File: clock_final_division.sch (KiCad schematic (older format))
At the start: 7 parts, among them SW2 SW_Rotary12, U10 74LVC161, U11 74LVC74, U9 74LVC74

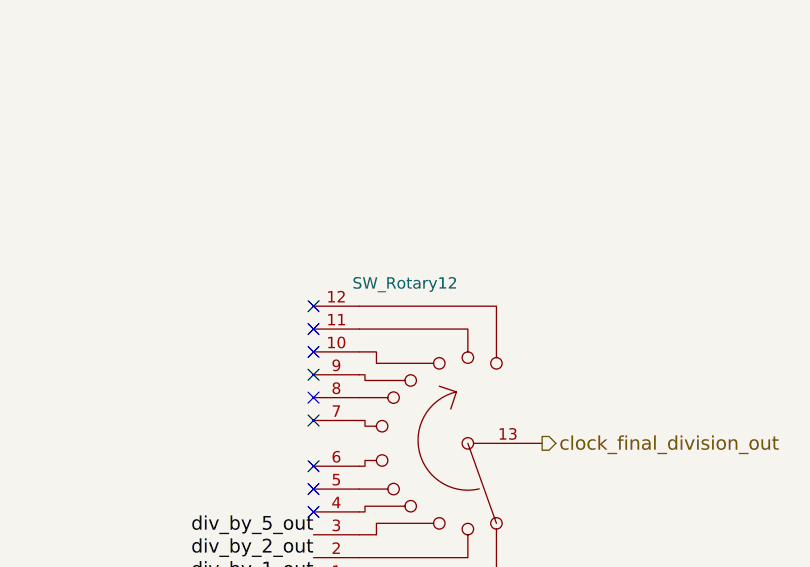
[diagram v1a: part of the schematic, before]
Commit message: R2 PCB rotary switches closer to middle of board
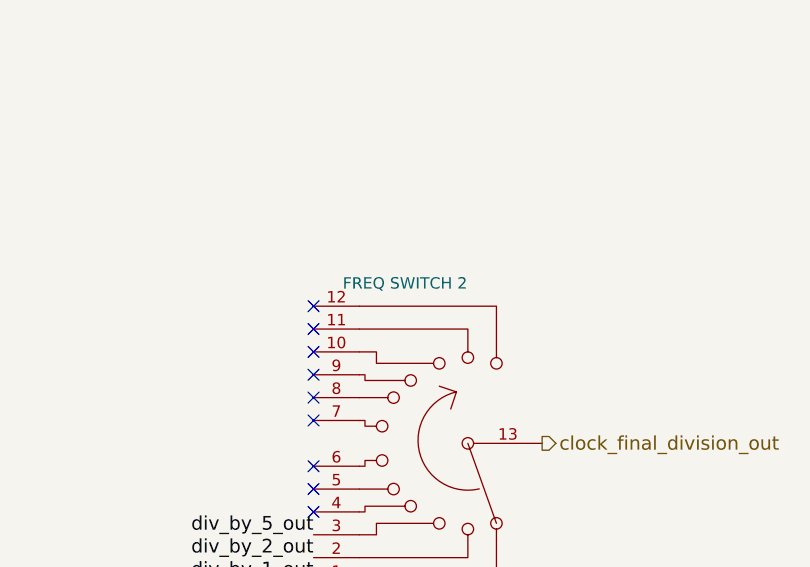
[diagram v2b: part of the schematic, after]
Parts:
- SW2: value SW_Rotary12 -> FREQ SWITCH 2; Distributor (none) -> Mouser; Distributor PN (none) -> 633-MRK112A; Manufacturer (none) -> NKK; Manufacturer PN (none) -> MRK112-A; URL (none) -> http://www.mouser.com/Search/ProductDetail.aspx?R=MRK112-Av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; Unit Price (none) -> 11.80
- U10: Distributor (none) -> Mouser; Distributor PN (none) -> 771-LVC161D118; Manufacturer (none) -> Nexperia; Manufacturer PN (none) -> 4LVC161D118; URL (none) -> http://www.mouser.com/Search/ProductDetail.aspx?R=74LVC161D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; Unit Price (none) -> 0.61
- U11, U9: Distributor (none) -> Mouser; Distributor PN (none) -> 595-SN74LVC74ADR; Manufacturer (none) -> TI; Manufacturer PN (none) -> SN74LVC74ADR; URL (none) -> http://www.mouser.com/Search/ProductDetail.aspx?R=SN74LVC74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; Unit Price (none) -> 0.40
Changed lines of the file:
@@
 encoding utf-8
 Sheet 3 6
-Title ""
+Title "calbox final frequency division"
 Date ""
 Rev ""
@@
 clock
 $Comp
-L GND #PWR33
+L GND #PWR032
 U 1 1 58C209C7
 P 1300 1500
-F 0 "#PWR33" H 1300 1250 50  0001 C CNN
+F 0 "#PWR032" H 1300 1250 50  0001 C CNN
 F 1 "GND" H 1300 1350 50  0000 C CNN
 F 2 "" H 1300 1500 50  0000 C CNN
@@
 $EndComp
 $Comp
-L GND #PWR41
+L GND #PWR033
 U 1 1 58C29AA8
 P 3800 1950
-F 0 "#PWR41" H 3800 1700 50  0001 C CNN
+F 0 "#PWR033" H 3800 1700 50  0001 C CNN
 F 1 "GND" H 3800 1800 50  0000 C CNN
 F 2 "" H 3800 1950 50  0000 C CNN
@@
 $EndComp
 $Comp
-L GND #PWR39
+L GND #PWR034
 U 1 1 58C29ADA
 P 3700 4650
-F 0 "#PWR39" H 3700 4400 50  0001 C CNN
+F 0 "#PWR034" H 3700 4400 50  0001 C CNN
 F 1 "GND" H 3700 4500 50  0000 C CNN
 F 2 "" H 3700 4650 50  0000 C CNN
@@
 $EndComp
 $Comp
-L GND #PWR47
+L GND #PWR035
 U 1 1 58C29B03
 P 7500 2950
-F 0 "#PWR47" H 7500 2700 50  0001 C CNN
+F 0 "#PWR035" H 7500 2700 50  0001 C CNN
 F 1 "GND" H 7500 2800 50  0000 C CNN
 F 2 "" H 7500 2950 50  0000 C CNN
@@
 clock
 $Comp
-L 74LVC161 U10
-U 1 1 58C76F32
-P 2300 1900
-F 0 "U10" H 2350 2000 50  0000 C CNN
-F 1 "74LVC161" H 2400 1700 50  0000 C CNN
-F 2 "SMD_Packages:SO-16-N" H 2300 1900 50  0001 C CNN
-F 3 "" H 2300 1900 50  0000 C CNN
-	1    2300 1900
-	1    0    0    -1
-$EndComp
-$Comp
 L 74LVC74 U9
 U 1 1 58C77242
@@
 F 1 "74LVC74" H 2300 3205 50  0000 C CNN
 F 2 "SMD_Packages:SOIC-14_N" H 2000 3500 50  0001 C CNN
-F 3 "" H 2000 3500 50  0000 C CNN
+F 3 "http://www.ti.com/lit/ds/symlink/sn74lvc74a.pdf" H 2000 3500 50  0001 C CNN
+F 4 "TI" H 2000 3500 60  0001 C CNN "Manufacturer"
+F 5 "SN74LVC74ADR" H 2000 3500 60  0001 C CNN "Manufacturer PN"
+F 6 "Mouser" H 2000 3500 60  0001 C CNN "Distributor"
+F 7 "595-SN74LVC74ADR" H 2000 3500 60  0001 C CNN "Distributor PN"
+F 8 "http://www.mouser.com/Search/ProductDetail.aspx?R=SN74LVC74ADRvirtualkey59500000virtualkey595-SN74LVC74ADR" H 2000 3500 60  0001 C CNN "URL"
+F 9 "0.40" H 2000 3500 60  0001 C CNN "Unit Price"
 	1    2000 3500
-	1    0    0    -1
-$EndComp
-$Comp
-L 74LVC74 U9
-U 2 1 58C7727E
-P 2000 5300
-F 0 "U9" H 2150 5600 50  0000 C CNN
-F 1 "74LVC74" H 2300 5005 50  0000 C CNN
-F 2 "SMD_Packages:SOIC-14_N" H 2000 5300 50  0001 C CNN
-F 3 "" H 2000 5300 50  0000 C CNN
-	2    2000 5300
-	1    0    0    -1
-$EndComp
-$Comp
-L 74LVC74 U11
-U 1 1 58C77320
-P 5900 1800
-F 0 "U11" H 6050 2100 50  0000 C CNN
-F 1 "74LVC74" H 6200 1505 50  0000 C CNN
-F 2 "SMD_Packages:SOIC-14_N" H 5900 1800 50  0001 C CNN
-F 3 "" H 5900 1800 50  0000 C CNN
-	1    5900 1800
-	1    0    0    -1
-$EndComp
-$Comp
-L 74LVC74 U11
-U 2 1 58C77357
-P 5900 3600
-F 0 "U11" H 6050 3900 50  0000 C CNN
-F 1 "74LVC74" H 6200 3305 50  0000 C CNN
-F 2 "SMD_Packages:SOIC-14_N" H 5900 3600 50  0001 C CNN
-F 3 "" H 5900 3600 50  0000 C CNN
-	2    5900 3600
 	1    0    0    -1
 $EndComp
@@
 P 8950 5300
 F 0 "SW2" H 8950 6000 50  0000 C CNN
-F 1 "SW_Rotary12" H 8950 4600 50  0000 C CNN
+F 1 "FREQ SWITCH 2" H 8950 4600 50  0000 C CNN
 F 2 "calbox:SW_ROTARY_SP12T_MRK112" H 8750 6000 50  0001 C CNN
-F 3 "" H 8750 6000 50  0001 C CNN
+F 3 "http://www.mouser.com/ds/2/295/MRlogicLevel-9701.pdf" H 8750 6000 50  0001 C CNN
+F 4 "NKK" H 8950 5300 60  0001 C CNN "Manufacturer"
+F 5 "MRK112-A" H 8950 5300 60  0001 C CNN "Manufacturer PN"
+F 6 "Mouser" H 8950 5300 60  0001 C CNN "Distributor"
+F 7 "633-MRK112A" H 8950 5300 60  0001 C CNN "Distributor PN"
+F 8 "http://www.mouser.com/Search/ProductDetail.aspx?R=MRK112-Avirtualkey63300000virtualkey633-MRK112A" H 8950 5300 60  0001 C CNN "URL"
+F 9 "11.80" H 8950 5300 60  0001 C CNN "Unit Price"
 	1    8950 5300
 	-1   0    0    1
@@
 NoConn ~ 8550 4700
 $Comp
-L VCC #PWR34
+L VCC #PWR036
 U 1 1 58C81CC4
 P 1800 4000
-F 0 "#PWR34" H 1800 3850 50  0001 C CNN
+F 0 "#PWR036" H 1800 3850 50  0001 C CNN
 F 1 "VCC" H 1800 4150 50  0000 C CNN
 F 2 "" H 1800 4000 50  0000 C CNN
@@
 $EndComp
 $Comp
-L VCC #PWR36
+L VCC #PWR037
 U 1 1 58C81F23
 P 2000 2950
-F 0 "#PWR36" H 2000 2800 50  0001 C CNN
+F 0 "#PWR037" H 2000 2800 50  0001 C CNN
 F 1 "VCC" H 2000 3100 50  0000 C CNN
 F 2 "" H 2000 2950 50  0000 C CNN
@@
 $EndComp
 $Comp
-L VCC #PWR37
+L VCC #PWR038
 U 1 1 58C81F49
 P 2000 4750
-F 0 "#PWR37" H 2000 4600 50  0001 C CNN
+F 0 "#PWR038" H 2000 4600 50  0001 C CNN
 F 1 "VCC" H 2000 4900 50  0000 C CNN
 F 2 "" H 2000 4750 50  0000 C CNN
@@
 $EndComp
 $Comp
-L VCC #PWR35
+L VCC #PWR039
 U 1 1 58C81F6F
 P 1800 5800
-F 0 "#PWR35" H 1800 5650 50  0001 C CNN
+F 0 "#PWR039" H 1800 5650 50  0001 C CNN
 F 1 "VCC" H 1800 5950 50  0000 C CNN
 F 2 "" H 1800 5800 50  0000 C CNN
@@
 $EndComp
 $Comp
-L VCC #PWR32
+L VCC #PWR040
 U 1 1 58C83204
 P 850 1900
-F 0 "#PWR32" H 850 1750 50  0001 C CNN
+F 0 "#PWR040" H 850 1750 50  0001 C CNN
 F 1 "VCC" H 850 2050 50  0000 C CNN
 F 2 "" H 850 1900 50  0000 C CNN
@@
 $EndComp
 $Comp
-L VCC #PWR40
+L VCC #PWR041
 U 1 1 58C8322A
 P 3800 1650
-F 0 "#PWR40" H 3800 1500 50  0001 C CNN
+F 0 "#PWR041" H 3800 1500 50  0001 C CNN
 F 1 "VCC" H 3800 1800 50  0000 C CNN
 F 2 "" H 3800 1650 50  0000 C CNN
@@
 $EndComp
 $Comp
-L VCC #PWR38
+L VCC #PWR042
 U 1 1 58C83250
 P 3700 4350
-F 0 "#PWR38" H 3700 4200 50  0001 C CNN
+F 0 "#PWR042" H 3700 4200 50  0001 C CNN
 F 1 "VCC" H 3700 4500 50  0000 C CNN
 F 2 "" H 3700 4350 50  0000 C CNN
@@
 $EndComp
 $Comp
-L VCC #PWR46
+L VCC #PWR043
 U 1 1 58C83276
 P 7500 2650
-F 0 "#PWR46" H 7500 2500 50  0001 C CNN
+F 0 "#PWR043" H 7500 2500 50  0001 C CNN
 F 1 "VCC" H 7500 2800 50  0000 C CNN
 F 2 "" H 7500 2650 50  0000 C CNN
@@
 $EndComp
 $Comp
-L VCC #PWR45
+L VCC #PWR044
 U 1 1 58C8329C
 P 5900 3050
-F 0 "#PWR45" H 5900 2900 50  0001 C CNN
+F 0 "#PWR044" H 5900 2900 50  0001 C CNN
 F 1 "VCC" H 5900 3200 50  0000 C CNN
 F 2 "" H 5900 3050 50  0000 C CNN
@@
 $EndComp
 $Comp
-L VCC #PWR44
+L VCC #PWR045
 U 1 1 58C832C2
 P 5900 1250
-F 0 "#PWR44" H 5900 1100 50  0001 C CNN
+F 0 "#PWR045" H 5900 1100 50  0001 C CNN
 F 1 "VCC" H 5900 1400 50  0000 C CNN
 F 2 "" H 5900 1250 50  0000 C CNN
@@
 $EndComp
 $Comp
-L VCC #PWR43
+L VCC #PWR046
 U 1 1 58C8357B
 P 5700 4100
-F 0 "#PWR43" H 5700 3950 50  0001 C CNN
+F 0 "#PWR046" H 5700 3950 50  0001 C CNN
 F 1 "VCC" H 5700 4250 50  0000 C CNN
 F 2 "" H 5700 4100 50  0000 C CNN
@@
 $EndComp
 $Comp
-L VCC #PWR42
+L VCC #PWR047
 U 1 1 58C835A1
 P 5700 2300
-F 0 "#PWR42" H 5700 2150 50  0001 C CNN
+F 0 "#PWR047" H 5700 2150 50  0001 C CNN
 F 1 "VCC" H 5700 2450 50  0000 C CNN
 F 2 "" H 5700 2300 50  0000 C CNN
@@
 	1    0    0    -1
 $EndComp
+$Comp
+L 74LVC161 U10
+U 1 1 58D05156
+P 2300 1900
+F 0 "U10" H 2350 2000 50  0000 C CNN
+F 1 "74LVC161" H 2400 1700 50  0000 C CNN
+F 2 "SMD_Packages:SO-16-N" H 2300 1900 50  0001 C CNN
+F 3 "http://www.mouser.com/ds/2/302/74LVC161-839606.pdf" H 2300 1900 50  0001 C CNN
+F 4 "Nexperia" H 2300 1900 60  0001 C CNN "Manufacturer"
+F 5 "4LVC161D118" H 2300 1900 60  0001 C CNN "Manufacturer PN"
+F 6 "Mouser" H 2300 1900 60  0001 C CNN "Distributor"
+F 7 "771-LVC161D118" H 2300 1900 60  0001 C CNN "Distributor PN"
+F 8 "http://www.mouser.com/Search/ProductDetail.aspx?R=74LVC161D%2c118virtualkey66800000virtualkey771-LVC161D118" H 2300 1900 60  0001 C CNN "URL"
+F 9 "0.61" H 2300 1900 60  0001 C CNN "Unit Price"
+	1    2300 1900
+	1    0    0    -1
+$EndComp
+$Comp
+L 74LVC74 U9
+U 2 1 58D05572
+P 2000 5300
+F 0 "U9" H 2150 5600 50  0000 C CNN
+F 1 "74LVC74" H 2300 5005 50  0000 C CNN
+F 2 "SMD_Packages:SOIC-14_N" H 2000 5300 50  0001 C CNN
+F 3 "http://www.ti.com/lit/ds/symlink/sn74lvc74a.pdf" H 2000 5300 50  0001 C CNN
+F 4 "TI" H 2000 5300 60  0001 C CNN "Manufacturer"
+F 5 "SN74LVC74ADR" H 2000 5300 60  0001 C CNN "Manufacturer PN"
+F 6 "Mouser" H 2000 5300 60  0001 C CNN "Distributor"
+F 7 "595-SN74LVC74ADR" H 2000 5300 60  0001 C CNN "Distributor PN"
+F 8 "http://www.mouser.com/Search/ProductDetail.aspx?R=SN74LVC74ADRvirtualkey59500000virtualkey595-SN74LVC74ADR" H 2000 5300 60  0001 C CNN "URL"
+F 9 "0.40" H 2000 5300 60  0001 C CNN "Unit Price"
+	2    2000 5300
+	1    0    0    -1
+$EndComp
+$Comp
+L 74LVC74 U11
+U 1 1 58D056BC
+P 5900 1800
+F 0 "U11" H 6050 2100 50  0000 C CNN
+F 1 "74LVC74" H 6200 1505 50  0000 C CNN
+F 2 "SMD_Packages:SOIC-14_N" H 5900 1800 50  0001 C CNN
+F 3 "http://www.ti.com/lit/ds/symlink/sn74lvc74a.pdf" H 5900 1800 50  0001 C CNN
+F 4 "TI" H 5900 1800 60  0001 C CNN "Manufacturer"
+F 5 "SN74LVC74ADR" H 5900 1800 60  0001 C CNN "Manufacturer PN"
+F 6 "Mouser" H 5900 1800 60  0001 C CNN "Distributor"
+F 7 "595-SN74LVC74ADR" H 5900 1800 60  0001 C CNN "Distributor PN"
+F 8 "http://www.mouser.com/Search/ProductDetail.aspx?R=SN74LVC74ADRvirtualkey59500000virtualkey595-SN74LVC74ADR" H 5900 1800 60  0001 C CNN "URL"
+F 9 "0.40" H 5900 1800 60  0001 C CNN "Unit Price"
+	1    5900 1800
+	1    0    0    -1
+$EndComp
+$Comp
+L 74LVC74 U11
+U 2 1 58D05720
+P 5900 3600
+F 0 "U11" H 6050 3900 50  0000 C CNN
+F 1 "74LVC74" H 6200 3305 50  0000 C CNN
+F 2 "SMD_Packages:SOIC-14_N" H 5900 3600 50  0001 C CNN
+F 3 "http://www.ti.com/lit/ds/symlink/sn74lvc74a.pdf" H 5900 3600 50  0001 C CNN
+F 4 "TI" H 5900 3600 60  0001 C CNN "Manufacturer"
+F 5 "SN74LVC74ADR" H 5900 3600 60  0001 C CNN "Manufacturer PN"
+F 6 "Mouser" H 5900 3600 60  0001 C CNN "Distributor"
+F 7 "595-SN74LVC74ADR" H 5900 3600 60  0001 C CNN "Distributor PN"
+F 8 "http://www.mouser.com/Search/ProductDetail.aspx?R=SN74LVC74ADRvirtualkey59500000virtualkey595-SN74LVC74ADR" H 5900 3600 60  0001 C CNN "URL"
+F 9 "0.40" H 5900 3600 60  0001 C CNN "Unit Price"
+	2    5900 3600
+	1    0    0    -1
+$EndComp

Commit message: update switch models in library, rotate final clock division switch
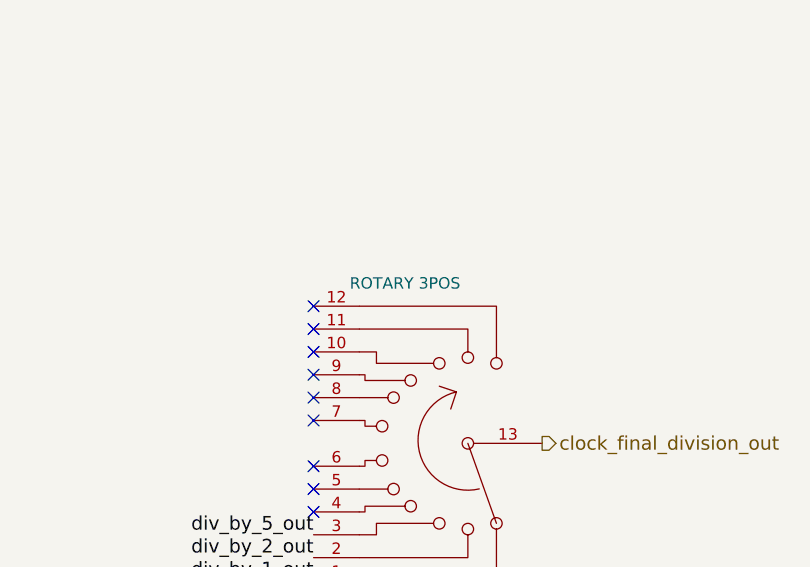
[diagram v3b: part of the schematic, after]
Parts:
- SW2: value FREQ SWITCH 2 -> ROTARY 3POS
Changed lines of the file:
@@
 P 8950 5300
 F 0 "SW2" H 8950 6000 50  0000 C CNN
-F 1 "FREQ SWITCH 2" H 8950 4600 50  0000 C CNN
+F 1 "ROTARY 3POS" H 8950 4600 50  0000 C CNN
 F 2 "calbox:SW_ROTARY_SP12T_MRK112" H 8750 6000 50  0001 C CNN
 F 3 "http://www.mouser.com/ds/2/295/MRlogicLevel-9701.pdf" H 8750 6000 50  0001 C CNN

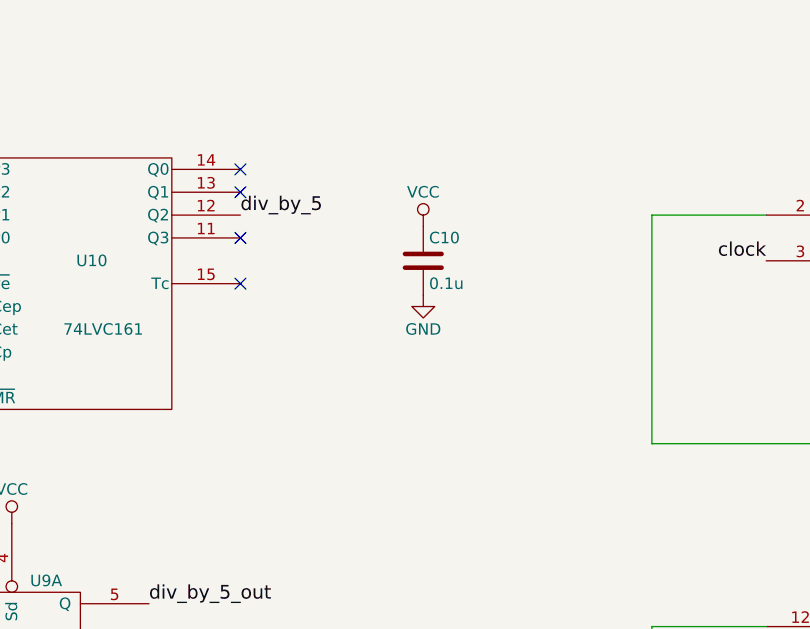
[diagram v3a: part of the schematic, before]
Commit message: Several schematic & layout changes after building first boards
- increase current limiting resistors on LEDs to make them less blinding
- add speedup cap, increase base resistor on voltage output switching
  transistor for better high frequency performance (should work up to 10MHz)
- change switched/constant voltage output toggle switch to actually work
  (now toggles between switched voltage output and constant voltage
  output, rather than switched and 0V output)
- add inverter to make div-by-5 circuit work
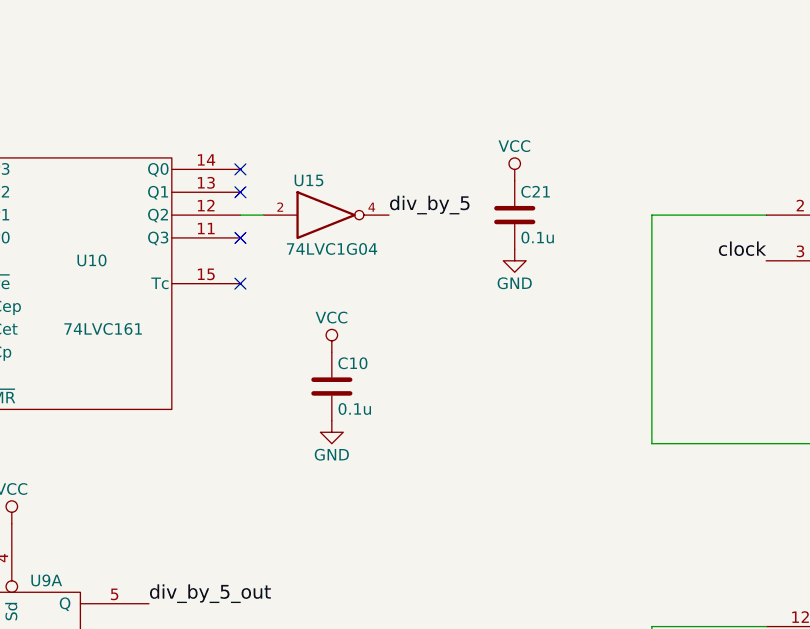
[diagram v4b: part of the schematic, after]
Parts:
- added C21: 0.1u, Capacitors_SMD:C_0805_HandSoldering, symbol C
- added U15: 74LVC1G04, TO_SOT_Packages_SMD:SOT-23-5, symbol 74LVC1G04
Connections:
- net GND: now also C21.2, U15.3 (GND)
- net VCC: now also C21.1, U15.5 (VCC)
- net div_by_5: now also U15.4; no longer U10.12 (Q2)
- new net: U10.12 (Q2), U15.2
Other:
- moved on the sheet: C10
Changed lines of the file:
@@
 NoConn ~ 3000 1400
 NoConn ~ 3000 1500
-Text Label 3000 1600 0    60   ~ 0
+Text Label 3650 1600 0    60   ~ 0
 div_by_5
 Text Label 1600 1900 2    60   ~ 0
@@
 L C C10
 U 1 1 58C29A9B
-P 3800 1800
-F 0 "C10" H 3825 1900 50  0000 L CNN
-F 1 "0.1u" H 3825 1700 50  0000 L CNN
-F 2 "Capacitors_SMD:C_0805_HandSoldering" H 3838 1650 50  0001 C CNN
-F 3 "" H 3800 1800 50  0000 C CNN
-	1    3800 1800
+P 3400 2350
+F 0 "C10" H 3425 2450 50  0000 L CNN
+F 1 "0.1u" H 3425 2250 50  0000 L CNN
+F 2 "Capacitors_SMD:C_0805_HandSoldering" H 3438 2200 50  0001 C CNN
+F 3 "" H 3400 2350 50  0000 C CNN
+	1    3400 2350
 	1    0    0    -1
 $EndComp
@@
 L GND #PWR033
 U 1 1 58C29AA8
-P 3800 1950
-F 0 "#PWR033" H 3800 1700 50  0001 C CNN
-F 1 "GND" H 3800 1800 50  0000 C CNN
-F 2 "" H 3800 1950 50  0000 C CNN
-F 3 "" H 3800 1950 50  0000 C CNN
-	1    3800 1950
+P 3400 2500
+F 0 "#PWR033" H 3400 2250 50  0001 C CNN
+F 1 "GND" H 3400 2350 50  0000 C CNN
+F 2 "" H 3400 2500 50  0000 C CNN
+F 3 "" H 3400 2500 50  0000 C CNN
+	1    3400 2500
 	1    0    0    -1
 $EndComp
@@
 L VCC #PWR041
 U 1 1 58C8322A
-P 3800 1650
-F 0 "#PWR041" H 3800 1500 50  0001 C CNN
-F 1 "VCC" H 3800 1800 50  0000 C CNN
-F 2 "" H 3800 1650 50  0000 C CNN
-F 3 "" H 3800 1650 50  0000 C CNN
-	1    3800 1650
+P 3400 2200
+F 0 "#PWR041" H 3400 2050 50  0001 C CNN
+F 1 "VCC" H 3400 2350 50  0000 C CNN
+F 2 "" H 3400 2200 50  0000 C CNN
+F 3 "" H 3400 2200 50  0000 C CNN
+	1    3400 2200
 	1    0    0    -1
 $EndComp
@@
 	1    0    0    -1
 $EndComp
+$Comp
+L 74LVC1G04 U15
+U 1 1 58F2DA98
+P 3400 1600
+F 0 "U15" H 3300 1750 50  0000 C CNN
+F 1 "74LVC1G04" H 3400 1450 50  0000 C CNN
+F 2 "TO_SOT_Packages_SMD:SOT-23-5" H 3400 1600 50  0001 C CNN
+F 3 "" H 3400 1600 50  0000 C CNN
+	1    3400 1600
+	1    0    0    -1
+$EndComp
+$Comp
+L C C21
+U 1 1 58F2DB21
+P 4200 1600
+F 0 "C21" H 4225 1700 50  0000 L CNN
+F 1 "0.1u" H 4225 1500 50  0000 L CNN
+F 2 "Capacitors_SMD:C_0805_HandSoldering" H 4238 1450 50  0001 C CNN
+F 3 "" H 4200 1600 50  0000 C CNN
+	1    4200 1600
+	1    0    0    -1
+$EndComp
+$Comp
+L GND #PWR048
+U 1 1 58F2DB27
+P 4200 1750
+F 0 "#PWR048" H 4200 1500 50  0001 C CNN
+F 1 "GND" H 4200 1600 50  0000 C CNN
+F 2 "" H 4200 1750 50  0000 C CNN
+F 3 "" H 4200 1750 50  0000 C CNN
+	1    4200 1750
+	1    0    0    -1
+$EndComp
+$Comp
+L VCC #PWR049
+U 1 1 58F2DB2D
+P 4200 1450
+F 0 "#PWR049" H 4200 1300 50  0001 C CNN
+F 1 "VCC" H 4200 1600 50  0000 C CNN
+F 2 "" H 4200 1450 50  0000 C CNN
+F 3 "" H 4200 1450 50  0000 C CNN
+	1    4200 1450
+	1    0    0    -1
+$EndComp
+Wire Wire Line
+	3000 1600 3100 1600
 $EndSCHEMATC
